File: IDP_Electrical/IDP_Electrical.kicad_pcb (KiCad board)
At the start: 2 copper layers, 25 parts, among them M1 DC Motor Symbol, M2 DC Motor Symbol, U1 SER0038, U2 SER0038

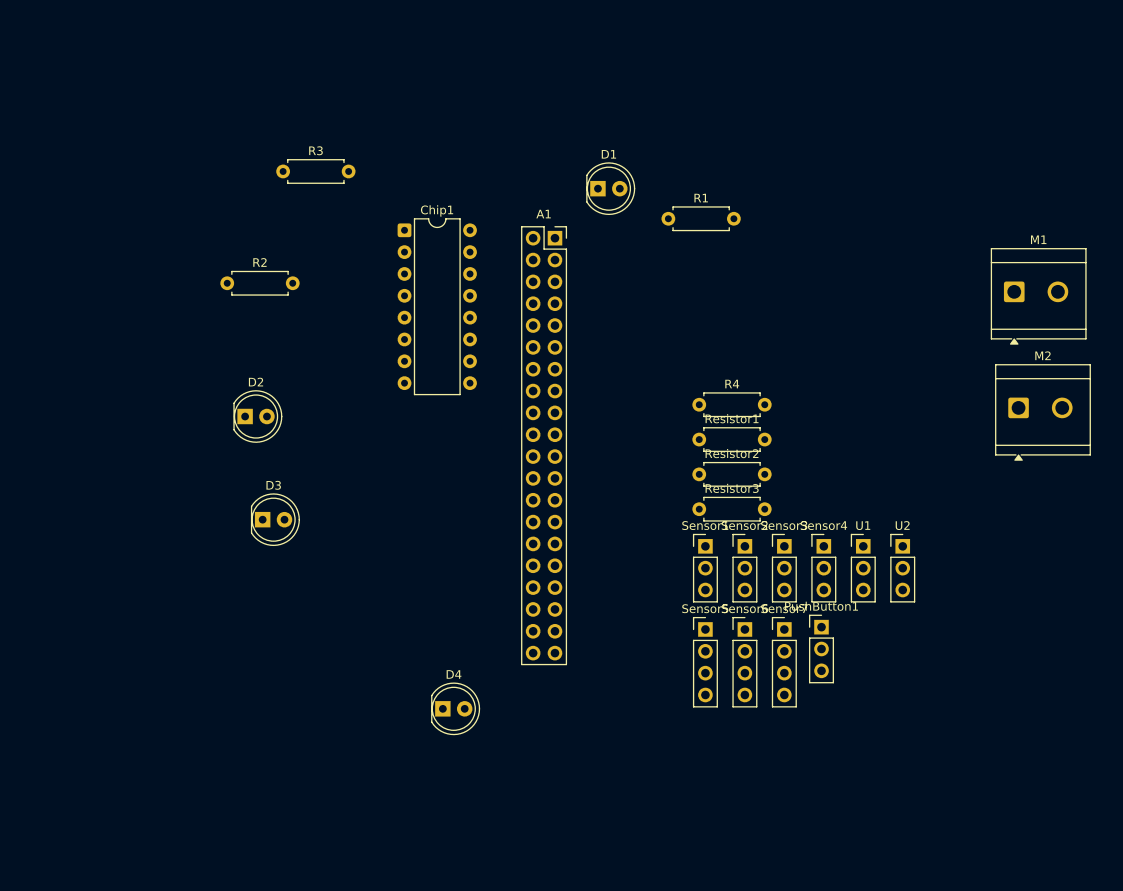
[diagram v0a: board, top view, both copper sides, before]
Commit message: updated power and ground
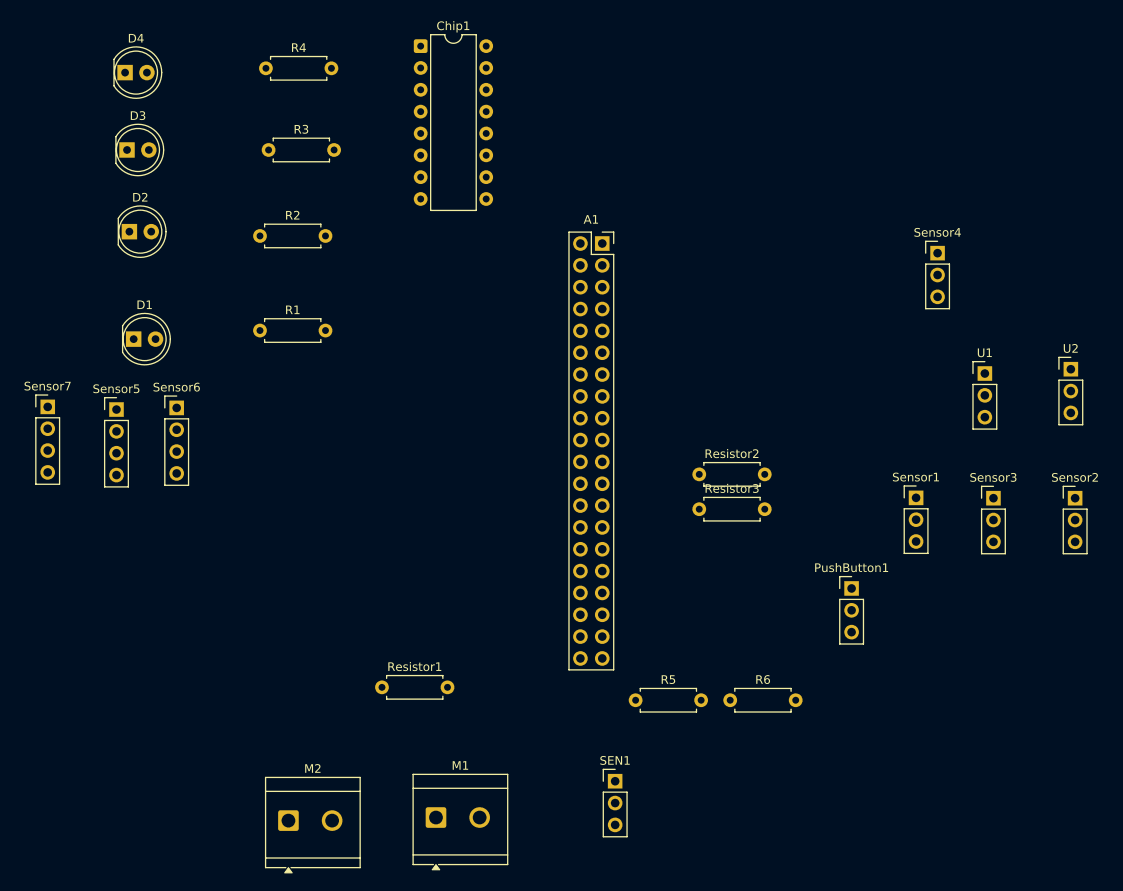
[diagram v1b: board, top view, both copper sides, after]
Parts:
- added R5: 2.2k, Resistor_THT:R_Axial_DIN0207_L6.3mm_D2.5mm_P7.62mm_Horizontal, F.Cu at (131.9, 108.5)
- added R6: R_test, Resistor_THT:R_Axial_DIN0207_L6.3mm_D2.5mm_P7.62mm_Horizontal, F.Cu at (142.9, 108.5)
- added SEN1: ~, Connector_PinHeader_2.54mm:PinHeader_1x03_P2.54mm_Vertical, F.Cu at (129.5, 117.9)
- moved M2 97.5 mm to (91.5, 122.5)
- moved M1 90.9 mm to (108.7, 122.1)
- moved Sensor7 89.5 mm to (63.5, 74.4)
- moved D4 82.7 mm to (72.5, 35.5)
- moved Sensor5 73.1 mm to (71.5, 74.7)
- moved Sensor6 70.9 mm to (78.5, 74.5)
- moved R4 63.8 mm to (88.9, 35.0)
- moved D1 56.8 mm to (73.5, 66.5)
- moved R1 49.2 mm to (88.2, 65.5)
- moved Resistor1 46.8 mm to (102.4, 107.0)
- moved D3 45.8 mm to (72.7, 44.5)
- moved Sensor2 38.8 mm to (183.0, 85.0)
- moved Sensor4 36.6 mm to (167.0, 56.5)
- moved U2 28.4 mm to (182.5, 70.0)
- moved D2 25.4 mm to (73.0, 54.0)
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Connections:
- R3 pad 1: Net-(Chip1-Pad1) -> Net-(Chip1-Pad1)_2
- R4 pad 1: Net-(Chip1-Pad1)_1 (its old number) -> Net-(Chip1-Pad1)

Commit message: updated schematic wiring
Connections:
- net Net-(D4-A) renamed +3V3
- Chip1 pad 15: Net-(Chip1-Pad15) -> GND
- Chip1 pad 2: Net-(Chip1-Pad15) -> GND
- Chip1 pad 3: Net-(Chip1-Pad3) -> GND
- Chip1 pad 7: Net-(Chip1-Pad15) -> GND
- PushButton1 pad 3: Net-(PushButton1-GND) -> GND
- R3 pad 1: Net-(Chip1-Pad1)_2 (its old number) -> Net-(Chip1-Pad1)
- R4 pad 1: Net-(Chip1-Pad1) -> Net-(Chip1-Pad1)_1
- R5 pad 1: Net-(SEN1-GND_Black) -> GND
- SEN1 pad 1: Net-(SEN1-GND_Black) -> GND
- Sensor1 pad 3: Net-(SEN1-GND_Black) -> GND
- Sensor2 pad 3: Net-(SEN1-GND_Black) -> GND
- Sensor3 pad 3: Net-(SEN1-GND_Black) -> GND
- Sensor4 pad 3: Net-(SEN1-GND_Black) -> GND
- Sensor5 pad 3: Net-(Sensor5-GND_Black) -> GND
- Sensor6 pad 3: Net-(Sensor5-GND_Black) -> GND
- Sensor7 pad 3: Net-(Sensor5-GND_Black) -> GND
- U1 pad 1: Net-(U1-GND) -> GND
- U2 pad 1: Net-(U2-GND) -> GND
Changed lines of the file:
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@@
 	(net 46 "Net-(M1--)")
 	(net 47 "Net-(M1-+)")
-	(net 48 "Net-(Chip1-Pad15)")
+	(net 48 "GND")
 	(net 49 "Net-(Chip1-Pad1)_2")
 	(net 50 "Net-(Chip1-Pad3)")
 	(net 51 "Net-(Chip1-Pad1)_1")
 	(net 52 "Net-(R5-Pad2)")
-	(net 53 "Net-(D4-A)")
+	(net 53 "+3V3")
 	(net 54 "Net-(M2--)")
 	(net 55 "Net-(M2-+)")
@@
 	(net 65 "Net-(Sensor5-Clock_Blue)")
 	(net 66 "Net-(Sensor5-Data_Green)")
-	(net 67 "Net-(U1-GND)")
-	(net 68 "Net-(U1-PWM)")
-	(net 69 "Net-(U1-Power_VCC)")
-	(net 70 "Net-(U2-GND)")
-	(net 71 "Net-(U2-PWM)")
-	(net 72 "Net-(U2-Power_VCC)")
-	(net 73 "Net-(SEN1-GND_Black)")
-	(net 74 "Net-(SEN1-Analog_Ouput_Blue)")
+	(net 67 "Net-(U1-PWM)")
+	(net 68 "Net-(U1-Power_VCC)")
+	(net 69 "Net-(U2-PWM)")
+	(net 70 "Net-(U2-Power_VCC)")
+	(net 71 "Net-(SEN1-Analog_Ouput_Blue)")
 	(footprint "Resistor_THT:R_Axial_DIN0207_L6.3mm_D2.5mm_P7.62mm_Horizontal"
 		(layer "F.Cu")
@@
 			(layers "*.Cu" "*.Mask")
 			(remove_unused_layers no)
-			(net 51 "Net-(Chip1-Pad1)_1")
+			(net 49 "Net-(Chip1-Pad1)_2")
 			(pintype "passive")
 		)
@@
 			(layers "*.Cu" "*.Mask")
 			(remove_unused_layers no)
-			(net 53 "Net-(D4-A)")
+			(net 53 "+3V3")
 			(pintype "passive")
 		)
@@
 			(layers "*.Cu" "*.Mask")
 			(remove_unused_layers no)
-			(net 15 "Net-(Sensor5-GND_Black)")
+			(net 48 "GND")
 			(pinfunction "GND_Black")
 			(pintype "power_in")
@@
 			(layers "*.Cu" "*.Mask")
 			(remove_unused_layers no)
-			(net 53 "Net-(D4-A)")
+			(net 53 "+3V3")
 			(pinfunction "3V3_Power_Red")
 			(pintype "power_in")
@@
 			(layers "*.Cu" "*.Mask")
 			(remove_unused_layers no)
-			(net 53 "Net-(D4-A)")
+			(net 53 "+3V3")
 			(pinfunction "A")
 			(pintype "passive")
@@
 			(layers "*.Cu" "*.Mask")
 			(remove_unused_layers no)
-			(net 70 "Net-(U2-GND)")
+			(net 48 "GND")
 			(pinfunction "GND")
 			(pintype "power_in")
@@
 			(layers "*.Cu" "*.Mask")
 			(remove_unused_layers no)
-			(net 72 "Net-(U2-Power_VCC)")
+			(net 70 "Net-(U2-Power_VCC)")
 			(pinfunction "Power_VCC")
 			(pintype "power_in")
@@
 			(layers "*.Cu" "*.Mask")
 			(remove_unused_layers no)
-			(net 71 "Net-(U2-PWM)")
+			(net 69 "Net-(U2-PWM)")
 			(pinfunction "PWM")
 			(pintype "input")
@@
 			(layers "*.Cu" "*.Mask")
 			(remove_unused_layers no)
-			(net 53 "Net-(D4-A)")
+			(net 53 "+3V3")
 			(pinfunction "3V3_Power_Red")
 			(pintype "power_in")
@@
 			(layers "*.Cu" "*.Mask")
 			(remove_unused_layers no)
-			(net 73 "Net-(SEN1-GND_Black)")
+			(net 48 "GND")
 			(pinfunction "GND_Black")
 			(pintype "power_in")
@@
 			(layers "*.Cu" "*.Mask")
 			(remove_unused_layers no)
-			(net 48 "Net-(Chip1-Pad15)")
+			(net 48 "GND")
 			(pintype "passive")
 		)
@@
 			(layers "*.Cu" "*.Mask")
 			(remove_unused_layers no)
-			(net 50 "Net-(Chip1-Pad3)")
+			(net 48 "GND")
 			(pintype "passive")
 		)
@@
 			(layers "*.Cu" "*.Mask")
 			(remove_unused_layers no)
-			(net 48 "Net-(Chip1-Pad15)")
+			(net 48 "GND")
 			(pintype "passive")
 		)
@@
 			(layers "*.Cu" "*.Mask")
 			(remove_unused_layers no)
-			(net 48 "Net-(Chip1-Pad15)")
+			(net 48 "GND")
 			(pintype "passive")
 		)
@@
 			(layers "*.Cu" "*.Mask")
 			(remove_unused_layers no)
-			(net 53 "Net-(D4-A)")
+			(net 53 "+3V3")
 			(pinfunction "3V3_Power_Red")
 			(pintype "power_in")
@@
 			(layers "*.Cu" "*.Mask")
 			(remove_unused_layers no)
-			(net 73 "Net-(SEN1-GND_Black)")
+			(net 48 "GND")
 			(pinfunction "GND_Black")
 			(pintype "power_in")
@@
 			(layers "*.Cu" "*.Mask")
 			(remove_unused_layers no)
-			(net 15 "Net-(Sensor5-GND_Black)")
+			(net 48 "GND")
 			(pinfunction "GND_Black")
 			(pintype "power_in")
@@
 			(layers "*.Cu" "*.Mask")
 			(remove_unused_layers no)
-			(net 53 "Net-(D4-A)")
+			(net 53 "+3V3")
 			(pinfunction "3V3_Power_Red")
 			(pintype "power_in")
@@
 			(layers "*.Cu" "*.Mask")
 			(remove_unused_layers no)
-			(net 38 "Net-(Chip1-Pad1)")
+			(net 51 "Net-(Chip1-Pad1)_1")
 			(pintype "passive")
 		)
@@
 			(layers "*.Cu" "*.Mask")
 			(remove_unused_layers no)
-			(net 15 "Net-(Sensor5-GND_Black)")
+			(net 48 "GND")
 			(pinfunction "GND_Black")
 			(pintype "power_in")
@@
 			(layers "*.Cu" "*.Mask")
 			(remove_unused_layers no)
-			(net 53 "Net-(D4-A)")
+			(net 53 "+3V3")
 			(pinfunction "3V3_Power_Red")
 			(pintype "power_in")
@@
 			(layers "*.Cu" "*.Mask")
 			(remove_unused_layers no)
-			(net 53 "Net-(D4-A)")
+			(net 53 "+3V3")
 			(pinfunction "3V3_Power_Red")
 			(pintype "power_in")
@@
 			(layers "*.Cu" "*.Mask")
 			(remove_unused_layers no)
-			(net 73 "Net-(SEN1-GND_Black)")
+			(net 48 "GND")
 			(pinfunction "GND_Black")
 			(pintype "power_in")
@@
 			(layers "*.Cu" "*.Mask")
 			(remove_unused_layers no)
-			(net 49 "Net-(Chip1-Pad1)_2")
+			(net 38 "Net-(Chip1-Pad1)")
 			(pintype "passive")
 		)
@@
 			(layers "*.Cu" "*.Mask")
 			(remove_unused_layers no)
-			(net 53 "Net-(D4-A)")
+			(net 53 "+3V3")
 			(pintype "passive")
 		)
@@
 			(layers "*.Cu" "*.Mask")
 			(remove_unused_layers no)
-			(net 67 "Net-(U1-GND)")
+			(net 48 "GND")
 			(pinfunction "GND")
 			(pintype "power_in")
@@
 			(layers "*.Cu" "*.Mask")
 			(remove_unused_layers no)
-			(net 69 "Net-(U1-Power_VCC)")
+			(net 68 "Net-(U1-Power_VCC)")
 			(pinfunction "Power_VCC")
 			(pintype "power_in")
@@
 			(layers "*.Cu" "*.Mask")
 			(remove_unused_layers no)
-			(net 68 "Net-(U1-PWM)")
+			(net 67 "Net-(U1-PWM)")
 			(pinfunction "PWM")
 			(pintype "input")
@@
 			(layers "*.Cu" "*.Mask")
 			(remove_unused_layers no)
-			(net 73 "Net-(SEN1-GND_Black)")
+			(net 48 "GND")
 			(pinfunction "GND_Black")
 			(pintype "power_in")
@@
 			(layers "*.Cu" "*.Mask")
 			(remove_unused_layers no)
-			(net 53 "Net-(D4-A)")
+			(net 53 "+3V3")
 			(pinfunction "3V3_Red")
 			(pintype "power_in")
@@
 			(layers "*.Cu" "*.Mask")
 			(remove_unused_layers no)
-			(net 74 "Net-(SEN1-Analog_Ouput_Blue)")
+			(net 71 "Net-(SEN1-Analog_Ouput_Blue)")
 			(pinfunction "Analog_Ouput_Blue")
 			(pintype "output")
@@
 			(layers "*.Cu" "*.Mask")
 			(remove_unused_layers no)
-			(net 53 "Net-(D4-A)")
+			(net 53 "+3V3")
 			(pintype "passive")
 		)
@@
 			(layers "*.Cu" "*.Mask")
 			(remove_unused_layers no)
-			(net 53 "Net-(D4-A)")
+			(net 53 "+3V3")
 			(pinfunction "3V3_Power")
 			(pintype "power_in")
@@
 			(layers "*.Cu" "*.Mask")
 			(remove_unused_layers no)
-			(net 16 "Net-(PushButton1-GND)")
+			(net 48 "GND")
 			(pinfunction "GND")
 			(pintype "power_in")
@@
 			(layers "*.Cu" "*.Mask")
 			(remove_unused_layers no)
-			(net 53 "Net-(D4-A)")
+			(net 53 "+3V3")
 			(pinfunction "3V3_Power_Red")
 			(pintype "power_in")
@@
 			(layers "*.Cu" "*.Mask")
 			(remove_unused_layers no)
-			(net 73 "Net-(SEN1-GND_Black)")
+			(net 48 "GND")
 			(pinfunction "GND_Black")
 			(pintype "power_in")
@@
 			(layers "*.Cu" "*.Mask")
 			(remove_unused_layers no)
-			(net 73 "Net-(SEN1-GND_Black)")
+			(net 48 "GND")
 			(pintype "passive")
 		)
@@
 			(layers "*.Cu" "*.Mask")
 			(remove_unused_layers no)
-			(net 53 "Net-(D4-A)")
+			(net 53 "+3V3")
 			(pintype "passive")
 		)
